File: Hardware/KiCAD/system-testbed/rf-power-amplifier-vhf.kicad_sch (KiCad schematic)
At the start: 0 parts

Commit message: feat: refine rf subsystem sheet, specify band selection from two tuned PAs #34
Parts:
- added C1, C43, C49: 1nF, symbol Device:C_US
- added C2: 10pF, symbol Device:C_US
- added C41, C45: 33pF, symbol Device:C_US
- added C44: 0.1uF, symbol Device:C_US
- added C46: 2.2nH, symbol Device:L
- added C47: 10uF, symbol Device:C_US
- added C48, C52: 27pF, symbol Device:C_US
- added C50, C53: 1.8pF, symbol Device:C_US
- added C54: 100pH, symbol Device:C_US
- added JP8: Single V_{CC}, Jumper:SolderJumper-2_P1.3mm_Open_RoundedPad1.0x1.5mm, symbol Jumper:SolderJumper_2_Bridged
- added L1: 10nH, symbol Device:L
- added L8: 20nH, symbol Device:L
- added L9: 23nH, symbol Device:L
- added R2: 1.96k, symbol Device:R_US
- added R34: 6.04k, symbol Device:R_US
- added R35: 0k, symbol Device:R_US
- added U1: GRF5604, Package_DFN_QFN:QFN-16-1EP_3x3mm_P0.5mm_EP1.7x1.7mm_ThermalVias, symbol capstone-project:GRF5604
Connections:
- new net: C46.2, C48.1, C50.1, C52.1, C53.1, C54.1
- new net: C45.1, C46.1, L9.2, U1.10 (RF_{OUT}), U1.9 (RF_{OUT})
- new net: R35.1, U1.12 (V_{BIAS})
- new net: C2.2, C41.1
- new net: C41.2, U1.3 (RF_{IN}), U1.4 (RF_{IN})
- new net: L8.2, U1.13 (V_{CC1})
- new net +5V: C44.1, JP8.1 (A), L8.1
- new net GND: C1.2, C43.2, C44.2, C45.2, C47.2, C48.2, C49.2, C50.2, C52.2, C53.2, L1.2, U1.11 (GND/NC), U1.14 (GND/NC), U1.17 (PAD), U1.2 (GND/NC), U1.5 (GND/NC), U1.6 (GND/NC), U1.7 (GND/NC), U1.8 (GND/NC)
- new net RF_{IN}: C2.1, L1.1
- new net RF_{OUT}: C54.2
- new net V_{CC2}: C47.1, C49.1, JP8.2 (B), L9.1, R35.2
- new net V_{ENABLE1}: C1.1, R2.1, R2.2, U1.16 (V_{ENABLE1})
- new net V_{ENABLE2}: C43.1, R34.1, R34.2, U1.15 (V_{ENABLE2})
- new net V_{SHUTDOWN}: U1.1 (V_{SHUTDOWN})
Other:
- note added: "**10 μF must be rated for > 5 V at maximum ambient temperature. Manufacturer Part Number in this case = GRM155C80J106ME11D."
- note added: "RF Amplifier for VHF Needs unique VHF Tune?"
- note added: "Single Supply M11 as JP7 V_{CC1} = V_{CC2}"

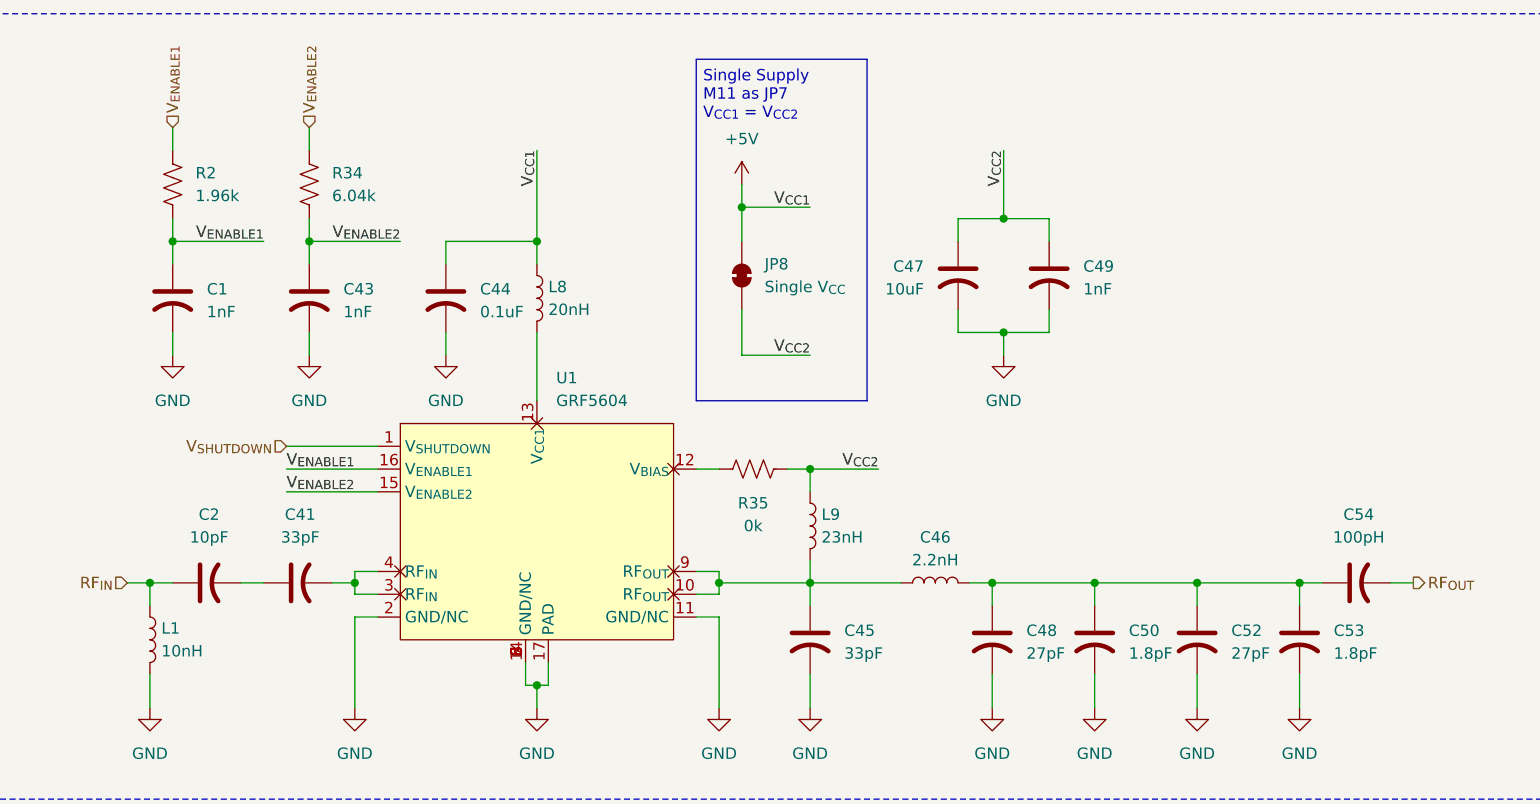
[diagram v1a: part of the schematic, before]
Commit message: feat: complete RF switches, revise RF sheet structure #34
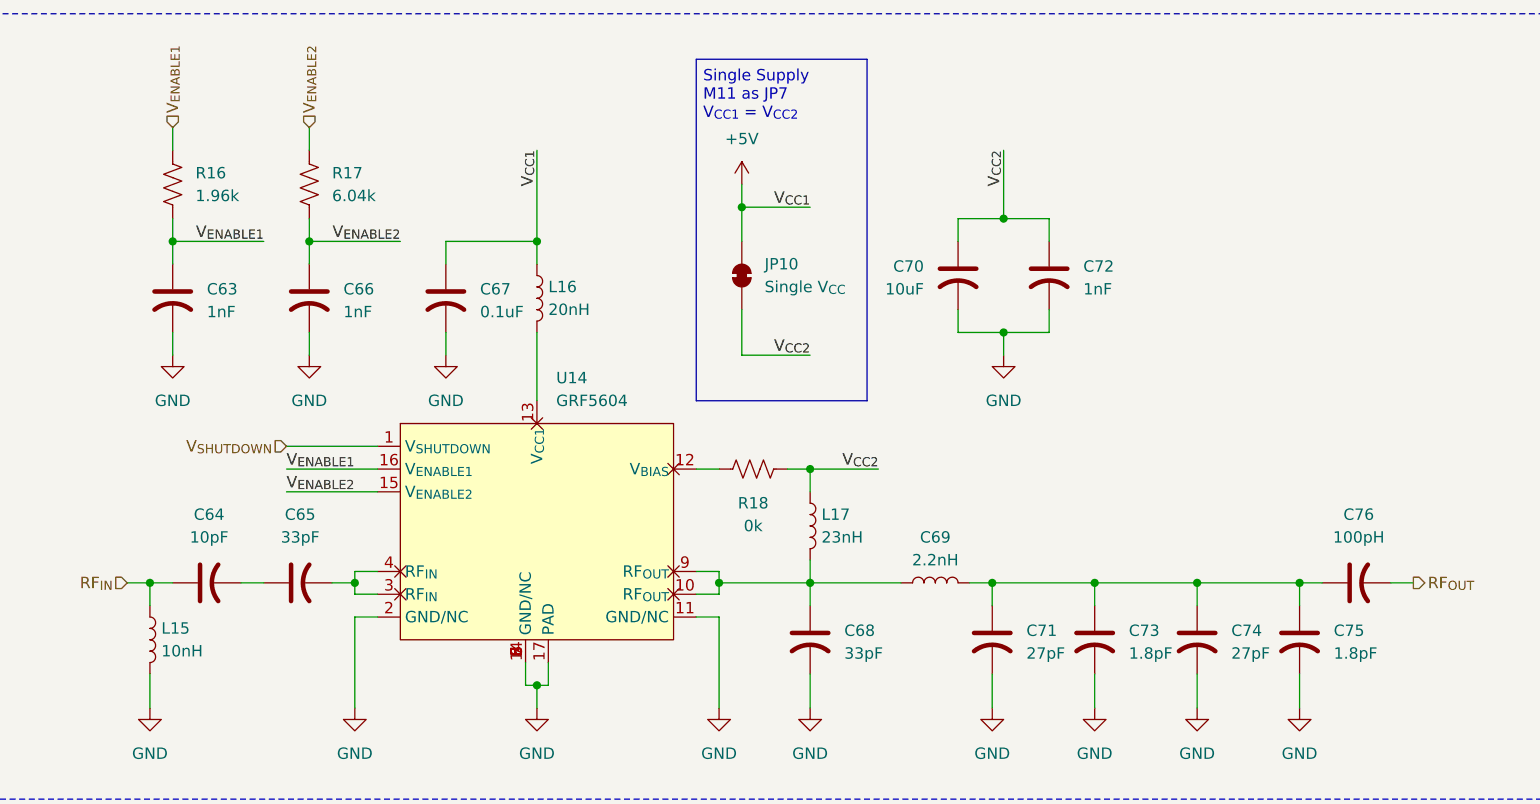
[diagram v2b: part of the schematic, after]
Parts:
- renumbered C1 to C63, C2 to C64, C41 to C65, C43 to C66, C44 to C67, C45 to C68, C46 to C69, C47 to C70, C48 to C71, C49 to C72, C50 to C73, C52 to C74, C53 to C75, C54 to C76, JP8 to JP10, L1 to L15, L8 to L16, L9 to L17, R2 to R16, R34 to R17, R35 to R18, U1 to U14
